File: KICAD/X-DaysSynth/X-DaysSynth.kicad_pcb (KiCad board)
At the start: 2 copper layers, 73 x 116 mm, 23 parts, among them J1 STYLUS, J2 Power Switch, J3 AudioJackX_Ground_Switch, J4 LED Ring, J5 PATCH SELECT, J6 WRITE PATCH, J7 PARAM SELECT, J8 MODE, J9 Power, U1 stm32f103c8t6-module-china

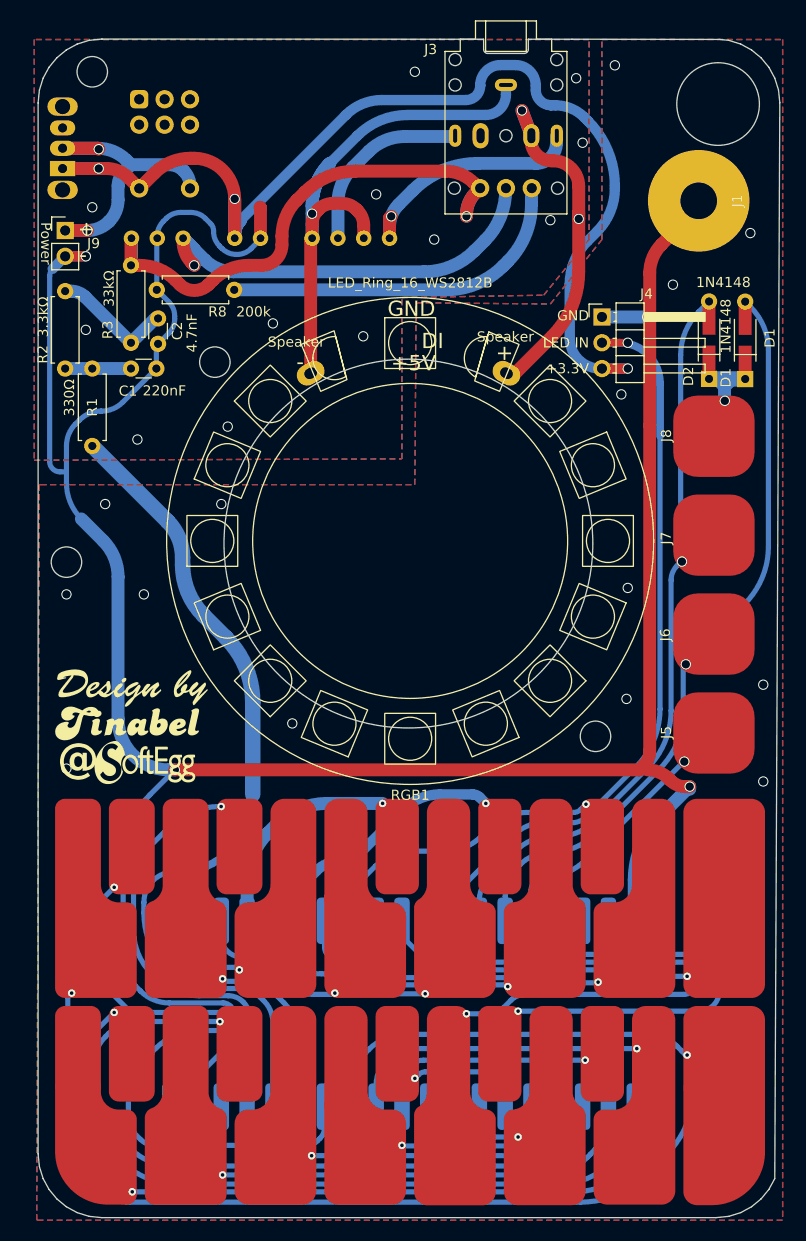
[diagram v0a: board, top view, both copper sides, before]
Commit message: LED ring 3d models updated PCB and schematic Logo Text first draft enclosures 3d models
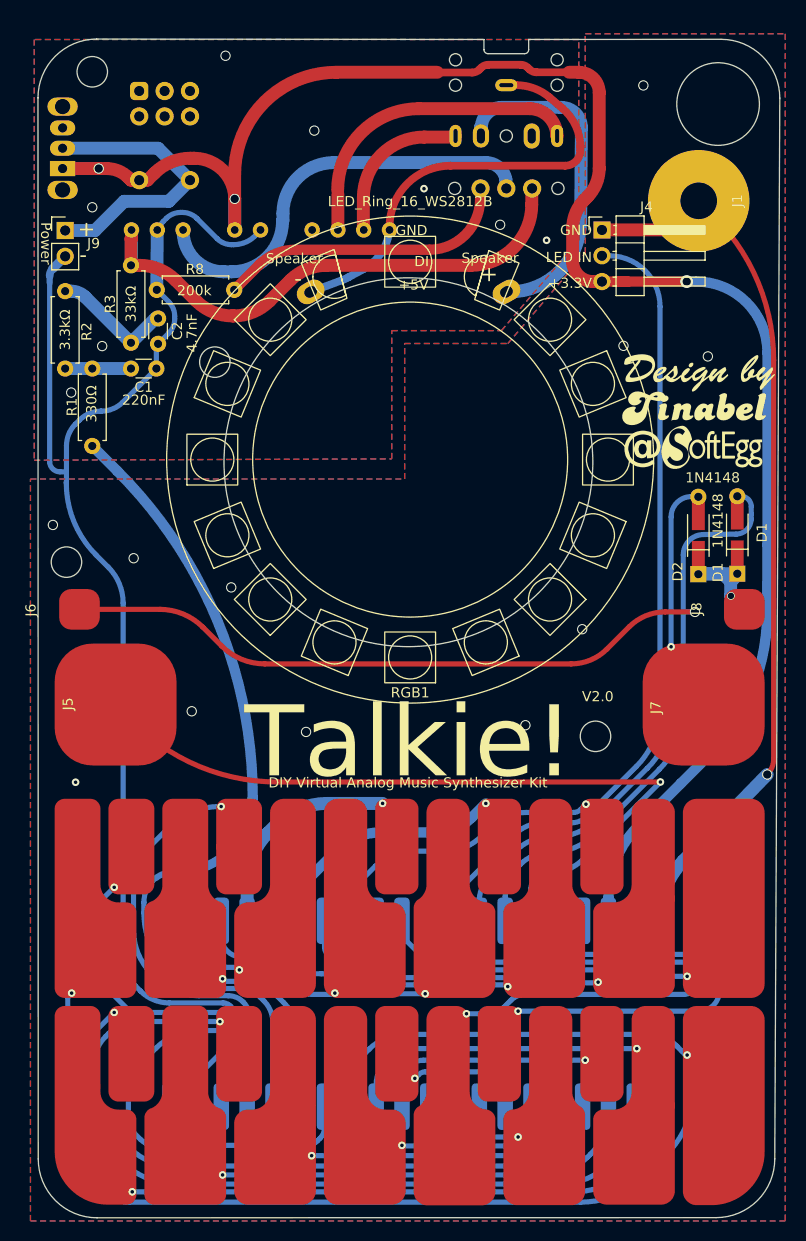
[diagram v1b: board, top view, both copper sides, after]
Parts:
- J3: moved to B.Cu
- moved J6 62.5 mm to (108.0, 103.5)
- moved J5 59.0 mm to (111.5, 110.5)
- moved D2 19.3 mm to (168.9, 97.7)
- moved D1 19.2 mm to (172.7, 97.7)
- moved J8 17.3 mm to (173.4, 101.2)
- moved J7 16.7 mm to (169.4, 114.0)
- moved J4 8.56 mm to (159.4, 63.8)
- moved LS1 8.00 mm to (140.3, 86.7)
- moved RGB1 8.00 mm to (140.5, 86.4)
- moved AMP1 0.81 mm to (138.5, 63.8)
- turned J3 to 0 degrees
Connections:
- AMP1 pad 1: Net-(AMP1-ROUT) -> Net-(AMP1-ROUT-)
- AMP1 pad 2: Net-(AMP1-LOUT-) -> Net-(AMP1-ROUT+)
- AMP1 pad 4: Net-(AMP1-LOUT-) -> unconnected-(AMP1-LOUT--Pad4)
- J3 pad G: Net-(AMP1-LOUT-) -> Net-(AMP1-ROUT-)
- J3 pad R: Net-(AMP1-ROUT) -> Net-(AMP1-ROUT+)
- LS1 pad 1: Net-(AMP1-LOUT-) -> Net-(AMP1-ROUT-)
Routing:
- net +3.3V: track 110.6 -> 180.4 mm
- net /PATCH: track 24.8 -> 77.5 mm
- net Net-(AMP1-LOUT-): track 52.2 -> 0.00 mm, vias 1 -> 0
- net /WRITE: track 74.9 -> 123.0 mm
- net /DGND: track 208.6 -> 163.9 mm, vias 17 -> 12
- net Net-(AMP1-ROUT-): track 0.00 -> 44.5 mm
- net Net-(AMP1-ROUT): track 24.2 -> 0.00 mm, vias 1 -> 0
- net /PARAM: track 73.4 -> 54.7 mm
- net Net-(AMP1-ROUT+): track 0.00 -> 15.7 mm
- net Net-(AMP1-LOUT+): track 18.4 -> 30.7 mm
- net Net-(J3-OUT): track 35.4 -> 29.3 mm
- net /LED_DIN: track 75.4 -> 81.0 mm, vias 1 -> 0
- net GNDA: track 45.5 -> 41.3 mm, vias 12 -> 5
- net /GND-IN: track 26.9 -> 22.8 mm, vias 1 -> 0
- net /C0: track 62.0 -> 58.0 mm
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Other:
- outline, holes or cut-outs redrawn
- board text added: "DIY Virtual Analog Music Synthesizer Kit"
- board text added: "Talkie!"
- board text added: "V2.0"
